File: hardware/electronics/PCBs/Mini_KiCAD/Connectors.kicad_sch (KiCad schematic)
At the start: 7 parts, among them J2 10118192-0001LF

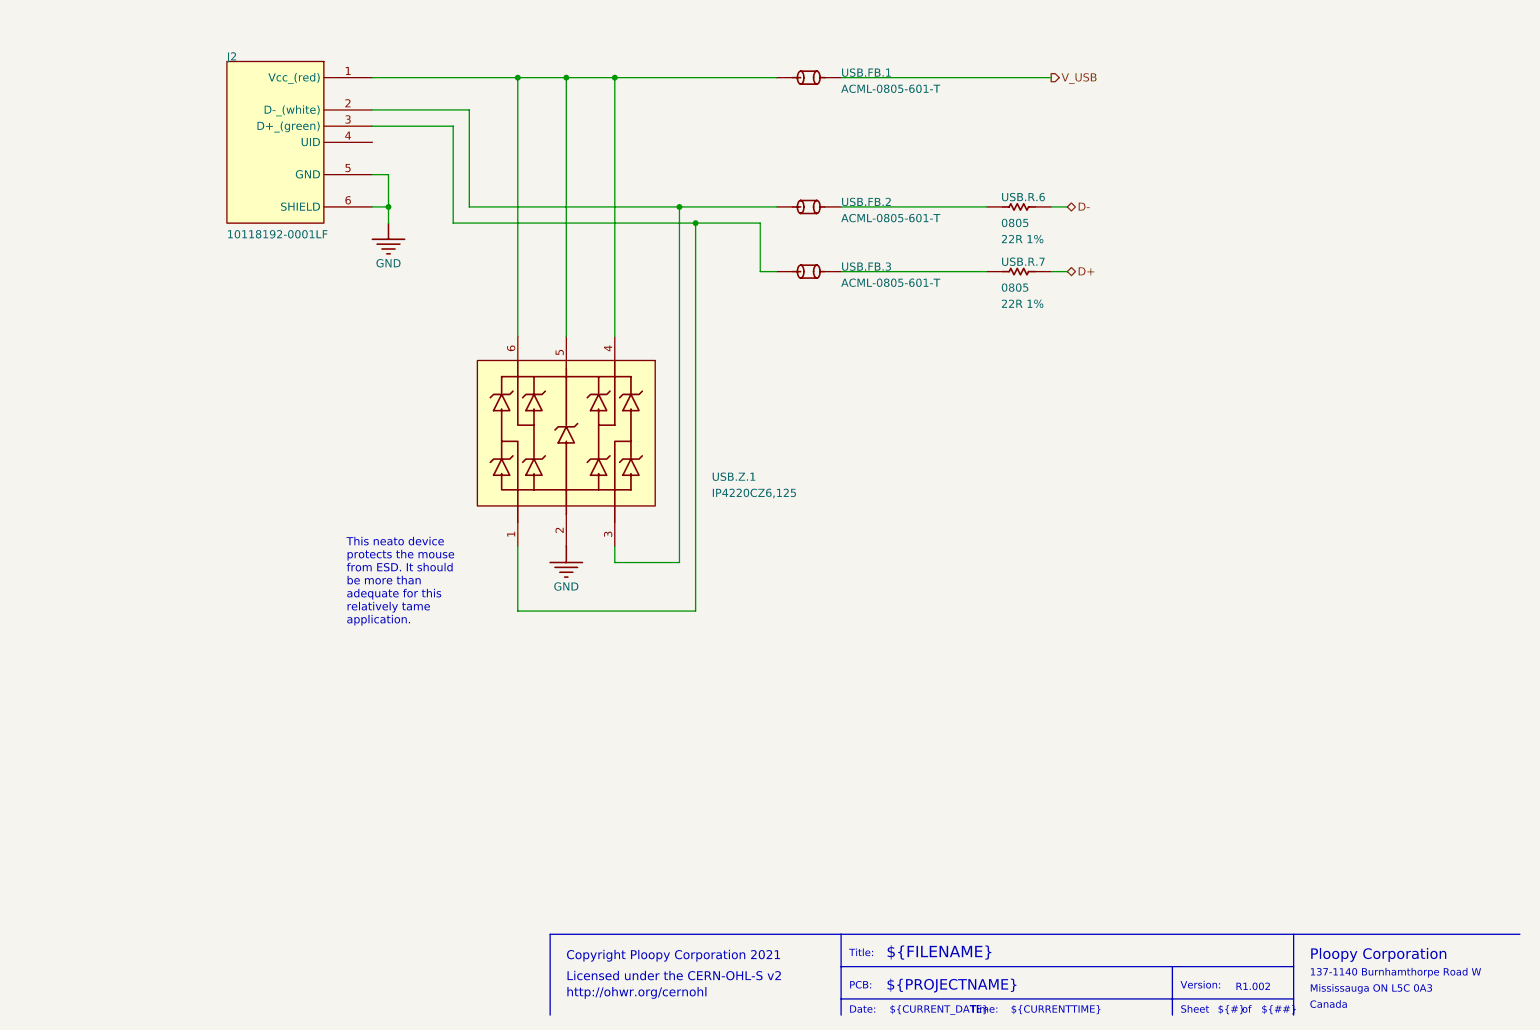
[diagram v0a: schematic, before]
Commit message: Initial commit of the modified Ploopy Mini PCB with RP2040, PMW3360 and mid-mounted USB-C
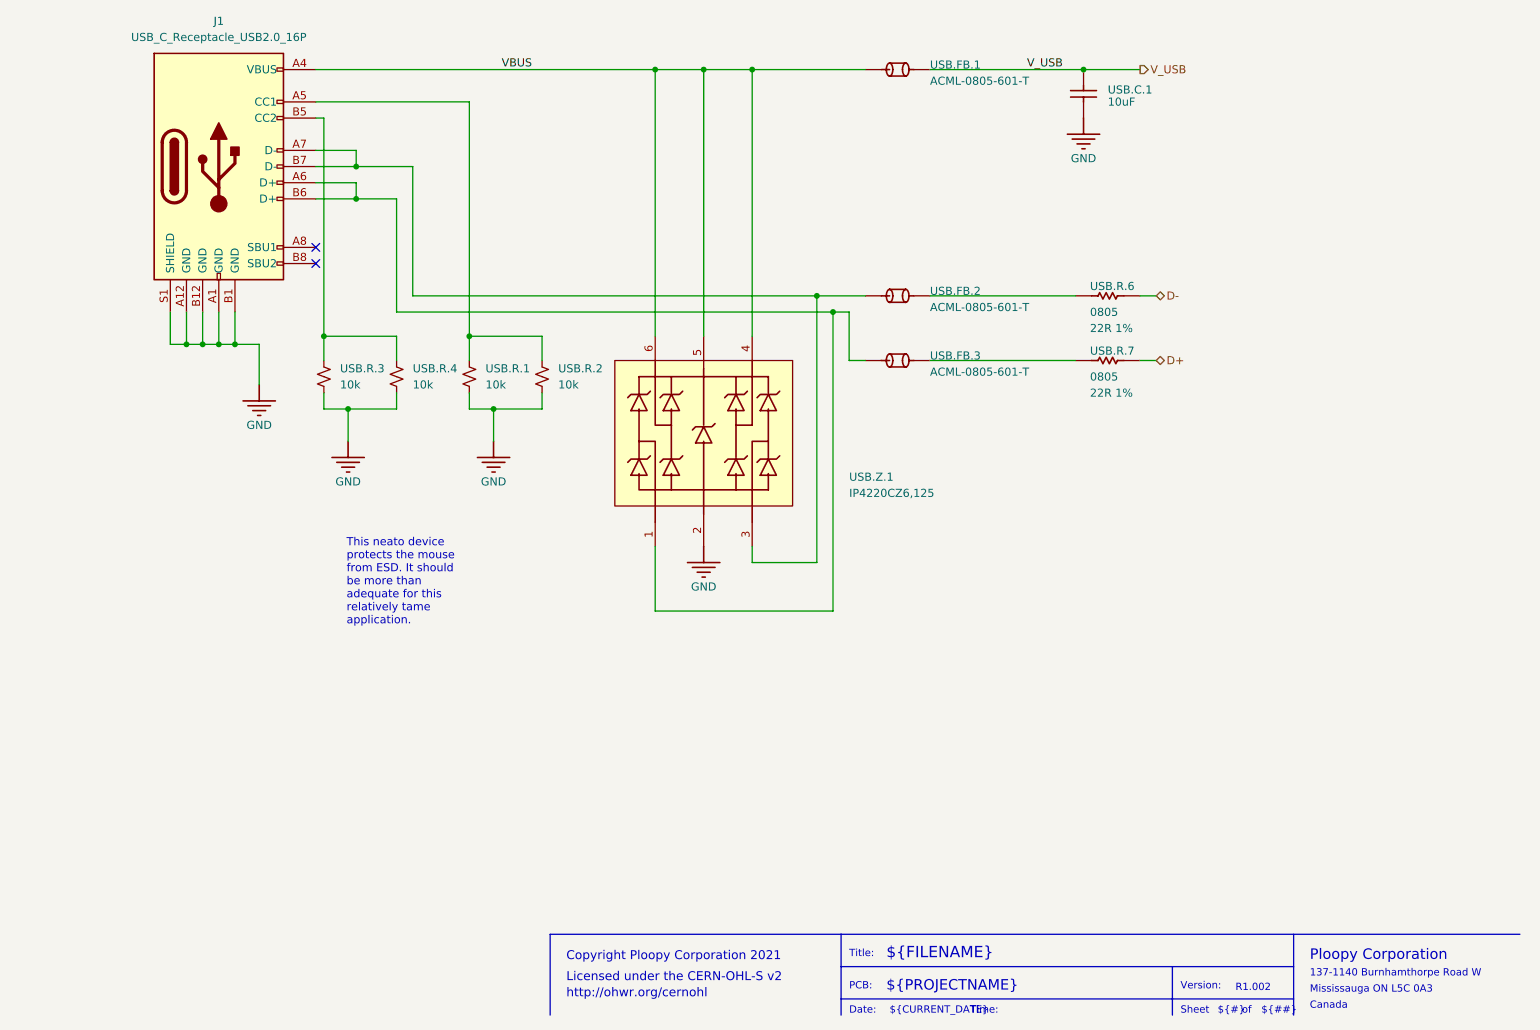
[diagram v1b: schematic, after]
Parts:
- removed J2: 10118192-0001LF, 10118192-0001LF, symbol Mini-altium-import:USB_0_mirrored_10118192-0001LF
- added J1: USB_C_Receptacle_USB2.0_16P, Connector:USB-C_2988367, symbol Connector:USB_C_Receptacle_USB2.0_16P
- added USB.C.1: 10uF, Chip_Passives.PcbLib:0805, symbol Mini-altium-import:MOS_1_Cap 10uF 25V
- added USB.R.1, USB.R.2, USB.R.3, USB.R.4: 10k, Chip_Passives.PcbLib:0805, symbol Device:R_Small_US
- USB.FB.1, USB.FB.2, USB.FB.3, USB.R.6, USB.R.7: footprint 0805 -> Chip_Passives.PcbLib:0805
- USB.Z.1: footprint PESD3V3S4UD - SOT95P275X110-6N -> Diodes.PcbLib:PESD3V3S4UD - SOT95P275X110-6N
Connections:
- net GND: now also J1.A1 (GND), J1.A12 (GND), J1.B1 (GND), J1.B12 (GND), J1.S1 (SHIELD), USB.C.1.1, USB.R.1.2, USB.R.2.2, USB.R.3.2, USB.R.4.2
- net V_USB: now also USB.C.1.2
- net at USB.FB.3.1, USB.Z.1.1: now also J1.A6 (D+), J1.B6 (D+)
- net at USB.FB.2.1, USB.Z.1.3: now also J1.A7 (D-), J1.B7 (D-)
- net VBUS: now reaches USB.FB.1.1, USB.Z.1.4, USB.Z.1.5, USB.Z.1.6
- net VBUS: now also J1.A4 (VBUS), J1.A9 (VBUS), J1.B4 (VBUS), J1.B9 (VBUS)
- new net: J1.B5 (CC2), USB.R.3.1, USB.R.4.1
- new net: J1.A5 (CC1), USB.R.1.1, USB.R.2.1
- no-connect marks 0 -> 2
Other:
- note removed: "${CURRENTTIME}"
- moved on the sheet: USB.FB.1, USB.FB.2, USB.FB.3, USB.R.6, USB.R.7, USB.Z.1

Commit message: Rerouted the SPI devices and general cleanup, relocated all associated footprint library inside the project folder
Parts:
- USB.C.1: footprint Chip_Passives.PcbLib:0805 -> Chip_Passives.PcbLib:0805 - TALL
- USB.Z.1: footprint Diodes.PcbLib:PESD3V3S4UD - SOT95P275X110-6N -> Diodes:PESD3V3S4UD - SOT95P275X110-6N
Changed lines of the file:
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@@
 			)
 		)
-		(property "Footprint" "Diodes.PcbLib:PESD3V3S4UD - SOT95P275X110-6N"
+		(property "Footprint" "Diodes:PESD3V3S4UD - SOT95P275X110-6N"
 			(at 146.05 119.38 0)
 			(effects
@@
 			)
 		)
-		(property "Footprint" "Chip_Passives.PcbLib:0805"
+		(property "Footprint" "Chip_Passives.PcbLib:0805 - TALL"
 			(at 203.2 67.31 0)
 			(effects

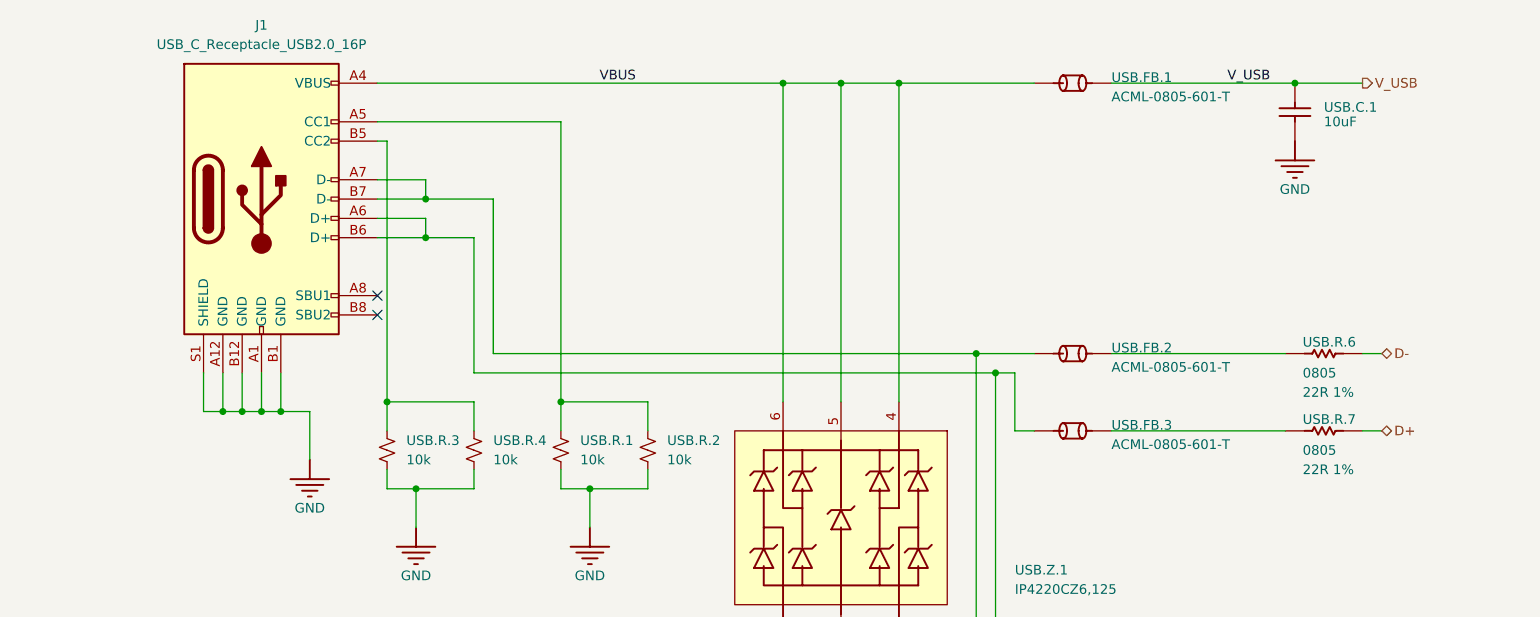
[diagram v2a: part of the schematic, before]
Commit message: Resolved most DRC errors and re-annotated the schematic to be friendly to BOM generation.
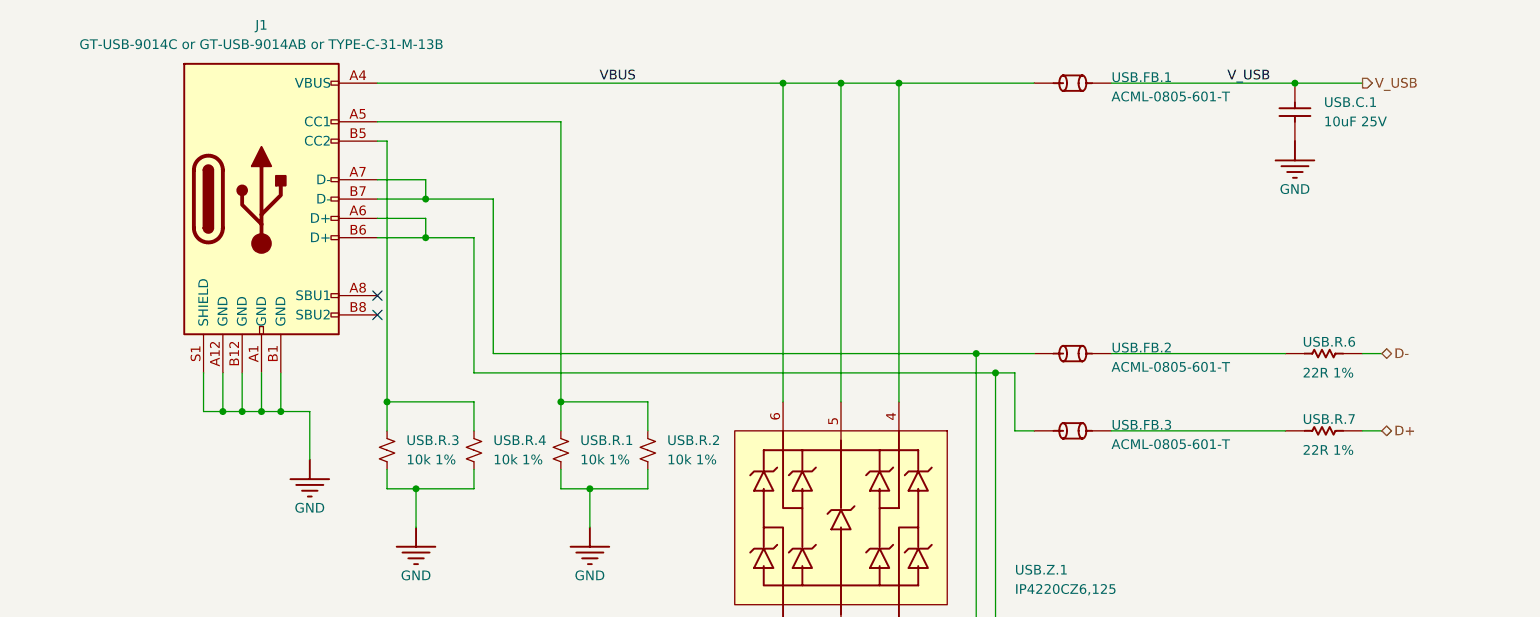
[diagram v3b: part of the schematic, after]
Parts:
- J1: value USB_C_Receptacle_USB2.0_16P -> GT-USB-9014C or GT-USB-9014AB or TYPE-C-31-M-13B
- USB.C.1: value 10uF -> 10uF 25V
- USB.R.1, USB.R.2, USB.R.3, USB.R.4: value 10k -> 10k 1%
- USB.R.6, USB.R.7: value 0805 -> 22R 1%
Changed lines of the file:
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@@
 			)
 		)
-		(property "Value" "0805"
+		(property "Value" "22R 1%"
 			(at 206.756 111.252 0)
 			(effects
@@
 				)
 				(justify left bottom)
+				(hide yes)
 			)
 		)
@@
 		(fields_autoplaced yes)
 		(property "Reference" "USB.C.1"
-			(at 209.55 65.4049 0)
+			(at 209.55 64.7699 0)
 			(effects
 				(font
@@
 			)
 		)
-		(property "Value" "10uF"
-			(at 209.55 67.31 0)
+		(property "Value" "10uF 25V"
+			(at 209.55 67.3099 0)
 			(effects
 				(font
@@
 			)
 		)
-		(property "Value" "10k"
+		(property "Value" "10k 1%"
 			(at 88.9 111.7599 0)
 			(effects
@@
 			)
 		)
-		(property "Value" "0805"
+		(property "Value" "22R 1%"
 			(at 206.756 101.092 0)
 			(effects
@@
 				)
 				(justify left bottom)
+				(hide yes)
 			)
 		)
@@
 			)
 		)
-		(property "Value" "10k"
+		(property "Value" "10k 1%"
 			(at 100.33 111.7599 0)
 			(effects
@@
 			)
 		)
-		(property "Value" "USB_C_Receptacle_USB2.0_16P"
+		(property "Value" "GT-USB-9014C or GT-USB-9014AB or TYPE-C-31-M-13B"
 			(at 69.85 57.15 0)
 			(effects
@@
 			)
 		)
-		(property "Value" "10k"
+		(property "Value" "10k 1%"
 			(at 123.19 111.7599 0)
 			(effects
@@
 			)
 		)
-		(property "Value" "10k"
+		(property "Value" "10k 1%"
 			(at 111.76 111.7599 0)
 			(effects

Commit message: Rev1.002 Replaced all symbols in the schematic with built-in symbols where applicable. Reoriented the sensor to solve interference and tracking issues. Replaced the mid-mount USB port with regular port.
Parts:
- J1: value GT-USB-9014C or GT-USB-9014AB or TYPE-C-31-M-13B -> TYPE-C-31-M-12; footprint Connector:USB-C_2988367 -> PCM_marbastlib-various:USB_C_Receptacle_HRO_TYPE-C-31-M-12
- USB.C.1: symbol Mini-altium-import:MOS_1_Cap 10uF 25V -> Device:C_Small
- USB.FB.1, USB.FB.2, USB.FB.3: symbol Mini-altium-import:USB_0_ACML-0805-601-T -> Device:FerriteBead
- USB.R.6, USB.R.7: symbol Mini-altium-import:USB_0_Res 22R 1% 0805 -> Device:R_Small_US
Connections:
- net UD+: now reaches J1.A6 (D+), J1.B6 (D+), USB.FB.3.1, USB.Z.1.1
- net UD-: now reaches J1.A7 (D-), J1.B7 (D-), USB.FB.2.1, USB.Z.1.3
